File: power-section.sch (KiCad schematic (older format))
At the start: 1 part, among them J1 Screw_Terminal_01x02

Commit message: Added MAX15062 as 3.3V power supply
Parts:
- added C?: C, symbol Device:C
- added C? (x2): 1uF, symbol Device:C
- added L?: 33uH, symbol Device:L
- added U?: MAX15062A, Package_DFN_QFN:DFN-8_2x2mm_P0.5mm, symbol Regulator_Switching:MAX15062A
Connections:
- net labels added: +24V, +3V3, 3.3V
- net labels removed: VCC
- wire segments 6 -> 31
- no-connect marks 0 -> 2
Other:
- moved on the sheet: J1

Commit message: Reorganized everything to use hierarchical sheets in KiCAD. Moved power supply section for motor driver into separate sheet. Moved connectors into top-level sheet
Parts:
- removed J1: Screw_Terminal_01x02, symbol Connector:Screw_Terminal_01x02
- added D1: SSC53L, symbol Device:D_Schottky
- C3: renamed from C?; value C -> 10uF
- gave numbers to parts that had none: 4
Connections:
- net labels added: 3V3, VIN
- net labels removed: +24V, +3V3, 3.3V
- wire segments 31 -> 27
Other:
- moved on the sheet: C1, C2, C3, L1, U1

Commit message: Generated annotations, netlists and assigned footprints into components
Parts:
- C1, C2, C3: footprint (none) -> Capacitor_SMD:C_0805_2012Metric_Pad1.15x1.40mm_HandSolder
- D1: footprint (none) -> Diode_SMD:D_SMC_Handsoldering
- L1: footprint (none) -> Inductor_SMD:L_Coilcraft_LPS4018
- U1: footprint Package_DFN_QFN:DFN-8_2x2mm_P0.5mm -> Package_DFN_QFN:DFN-8-1EP_2x2mm_P0.5mm_EP0.9x1.5mm
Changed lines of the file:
@@
 F 0 "U1" H 6050 4067 50  0000 C CNN
 F 1 "MAX15062A" H 6050 3976 50  0000 C CNN
-F 2 "Package_DFN_QFN:DFN-8_2x2mm_P0.5mm" H 6050 4150 50  0001 C CIN
+F 2 "Package_DFN_QFN:DFN-8-1EP_2x2mm_P0.5mm_EP0.9x1.5mm" H 6050 4150 50  0001 C CIN
 F 3 "http://datasheets.maximintegrated.com/en/ds/MAX15062.pdf" H 6050 3550 50  0001 C CNN
 	1    6050 3600
@@
 F 0 "L1" V 6990 3400 50  0000 C CNN
 F 1 "33uH" V 6899 3400 50  0000 C CNN
-F 2 "" H 6800 3400 50  0001 C CNN
+F 2 "Inductor_SMD:L_Coilcraft_LPS4018" H 6800 3400 50  0001 C CNN
 F 3 "~" H 6800 3400 50  0001 C CNN
 	1    6800 3400
@@
 F 0 "C3" H 7165 4096 50  0000 L CNN
 F 1 "10uF" H 7165 4005 50  0000 L CNN
-F 2 "" H 7088 3900 50  0001 C CNN
+F 2 "Capacitor_SMD:C_0805_2012Metric_Pad1.15x1.40mm_HandSolder" H 7088 3900 50  0001 C CNN
 F 3 "~" H 7050 4050 50  0001 C CNN
 	1    7050 4050
@@
 F 0 "C2" H 5565 4096 50  0000 L CNN
 F 1 "1uF" H 5565 4005 50  0000 L CNN
-F 2 "" H 5488 3900 50  0001 C CNN
+F 2 "Capacitor_SMD:C_0805_2012Metric_Pad1.15x1.40mm_HandSolder" H 5488 3900 50  0001 C CNN
 F 3 "~" H 5450 4050 50  0001 C CNN
 	1    5450 4050
@@
 F 0 "C1" H 5315 3696 50  0000 L CNN
 F 1 "1uF" H 5315 3605 50  0000 L CNN
-F 2 "" H 5238 3500 50  0001 C CNN
+F 2 "Capacitor_SMD:C_0805_2012Metric_Pad1.15x1.40mm_HandSolder" H 5238 3500 50  0001 C CNN
 F 3 "~" H 5200 3650 50  0001 C CNN
 	1    5200 3650
@@
 F 0 "D1" H 4900 3200 50  0000 L CNN
 F 1 "SSC53L" H 4800 3300 50  0000 L CNN
-F 2 "" H 4950 3400 50  0001 C CNN
+F 2 "Diode_SMD:D_SMC_Handsoldering" H 4950 3400 50  0001 C CNN
 F 3 "~" H 4950 3400 50  0001 C CNN
 	1    4950 3400

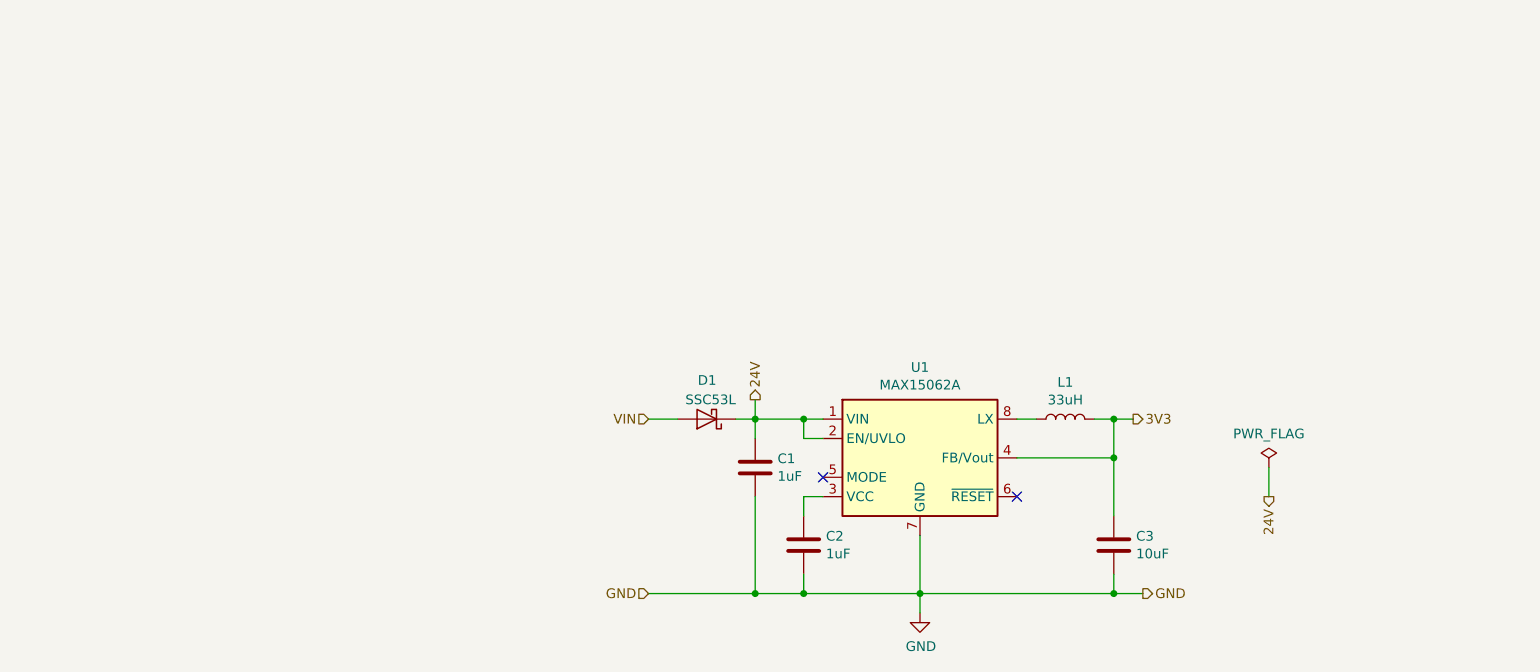
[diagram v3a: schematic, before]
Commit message: Added power supply section to PCB. Added missing components footprints.
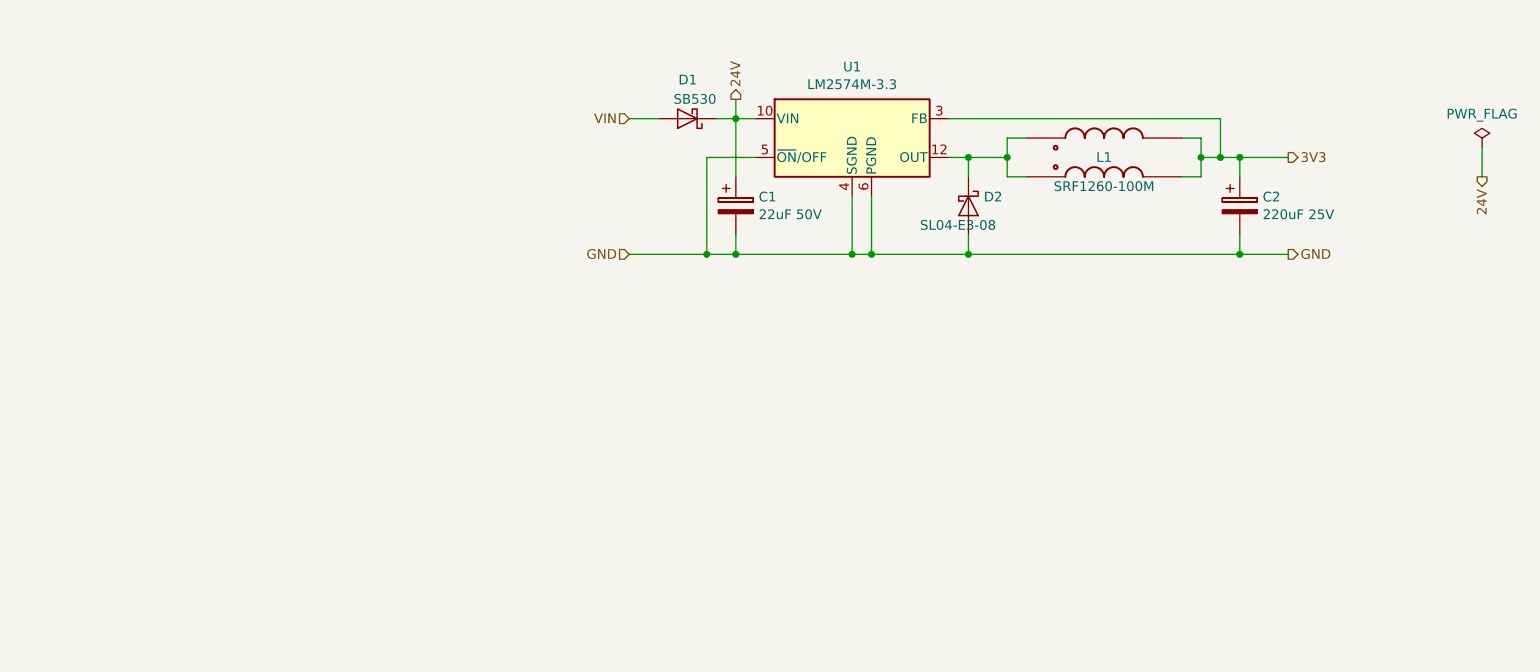
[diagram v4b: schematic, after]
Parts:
- removed C1, C2: 1uF, Capacitor_SMD:C_0805_2012Metric_Pad1.15x1.40mm_HandSolder, symbol Device:C
- removed C3: 10uF, Capacitor_SMD:C_0805_2012Metric_Pad1.15x1.40mm_HandSolder, symbol Device:C
- removed L1: 33uH, Inductor_SMD:L_Coilcraft_LPS4018, symbol Device:L
- removed U1: MAX15062A, Package_DFN_QFN:DFN-8-1EP_2x2mm_P0.5mm_EP0.9x1.5mm, symbol Regulator_Switching:MAX15062A
- added C1: 22uF 50V, Capacitor_THT:CP_Radial_D5.0mm_P2.00mm, symbol Device:CP
- added C2: 220uF 25V, Capacitor_THT:CP_Radial_D6.3mm_P2.50mm, symbol Device:CP
- added D2: SL04-E3-08, Diode_SMD:D_1210_3225Metric_Pad1.42x2.65mm_HandSolder, symbol Device:D_Schottky
- added L1: SRF1260-100M, IND_SRF1260-100M, symbol SRF1260-100M:SRF1260-100M
- added U1: LM2574M-3.3, Package_SO:SOIC-14W_7.5x9.0mm_P1.27mm, symbol Regulator_Switching:LM2574M-3.3
- D1: value SSC53L -> SB530; footprint Diode_SMD:D_SMC_Handsoldering -> Diode_THT:D_DO-201_P3.81mm_Vertical_AnodeUp
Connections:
- net 24V: now also C1.1, U1.10 (VIN)
- net 3V3: now also C2.1, L1.3, L1.4, U1.3 (FB)
- net GND: now also C1.2, C2.2, D2.2 (A), U1.4 (SGND), U1.5 (~ON~/OFF), U1.6 (PGND)
- new net: D2.1 (K), L1.1, L1.2, U1.12 (OUT)
- no-connect marks 2 -> 0
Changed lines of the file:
@@
 Comment4 ""
 $EndDescr
+Text HLabel 7950 2050 2    50   Output ~ 0
+3V3
+Wire Wire Line
+	4550 1850 4700 1850
+Text HLabel 7950 2550 2    50   Output ~ 0
+GND
+Text HLabel 4550 2550 0    50   Input ~ 0
+GND
+Text HLabel 4550 1850 0    50   Input ~ 0
+VIN
+Text HLabel 5100 1750 1    50   Output ~ 0
+24V
 $Comp
-L Regulator_Switching:MAX15062A U1
-U 1 1 5BD97FD1
-P 6050 3600
-F 0 "U1" H 6050 4067 50  0000 C CNN
-F 1 "MAX15062A" H 6050 3976 50  0000 C CNN
-F 2 "Package_DFN_QFN:DFN-8-1EP_2x2mm_P0.5mm_EP0.9x1.5mm" H 6050 4150 50  0001 C CIN
-F 3 "http://datasheets.maximintegrated.com/en/ds/MAX15062.pdf" H 6050 3550 50  0001 C CNN
-	1    6050 3600
+L Device:D_Schottky D1
+U 1 1 5BE562E4
+P 4850 1850
+AR Path="/5BDAF501/5BE562E4" Ref="D1"  Part="1"
+AR Path="/5BE562E4" Ref="D?"  Part="1"
+F 0 "D1" H 4800 1650 50  0000 L CNN
+F 1 "SB530" H 4700 1750 50  0000 L CNN
+F 2 "Diode_THT:D_DO-201_P3.81mm_Vertical_AnodeUp" H 4850 1850 50  0001 C CNN
+F 3 "~" H 4850 1850 50  0001 C CNN
+	1    4850 1850
+	-1   0    0    1
+$EndComp
+$Comp
+L power:PWR_FLAG #FLG01
+U 1 1 5BE562EB
+P 8950 2000
+F 0 "#FLG01" H 8950 2075 50  0001 C CNN
+F 1 "PWR_FLAG" H 8950 2174 50  0000 C CNN
+F 2 "" H 8950 2000 50  0001 C CNN
+F 3 "~" H 8950 2000 50  0001 C CNN
+	1    8950 2000
 	1    0    0    -1
 $EndComp
+Text HLabel 8950 2150 3    50   Output ~ 0
+24V
+Wire Wire Line
+	8950 2150 8950 2000
 $Comp
-L Device:L L1
-U 1 1 5BD98297
-P 6800 3400
-F 0 "L1" V 6990 3400 50  0000 C CNN
-F 1 "33uH" V 6899 3400 50  0000 C CNN
-F 2 "Inductor_SMD:L_Coilcraft_LPS4018" H 6800 3400 50  0001 C CNN
-F 3 "~" H 6800 3400 50  0001 C CNN
-	1    6800 3400
-	0    -1   -1   0
-$EndComp
-Wire Wire Line
-	6550 3400 6650 3400
-$Comp
-L Device:C C3
-U 1 1 5BD98368
-P 7050 4050
-F 0 "C3" H 7165 4096 50  0000 L CNN
-F 1 "10uF" H 7165 4005 50  0000 L CNN
-F 2 "Capacitor_SMD:C_0805_2012Metric_Pad1.15x1.40mm_HandSolder" H 7088 3900 50  0001 C CNN
-F 3 "~" H 7050 4050 50  0001 C CNN
-	1    7050 4050
+L Regulator_Switching:LM2574M-3.3 U1
+U 1 1 5BE562F3
+P 5700 1950
+F 0 "U1" H 5700 2317 50  0000 C CNN
+F 1 "LM2574M-3.3" H 5700 2226 50  0000 C CNN
+F 2 "Package_SO:SOIC-14W_7.5x9.0mm_P1.27mm" H 5300 2300 50  0001 L CIN
+F 3 "http://www.national.com/ds/LM/LM2574.pdf" H 5700 1950 50  0001 C CNN
+	1    5700 1950
 	1    0    0    -1
 $EndComp
 Wire Wire Line
-	6050 4000 6050 4300
-Wire Wire Line
-	6050 4300 7050 4300
-Wire Wire Line
-	7050 4300 7050 4200
+	5000 1850 5100 1850
 $Comp
-L Device:C C2
-U 1 1 5BD984C8
-P 5450 4050
-F 0 "C2" H 5565 4096 50  0000 L CNN
-F 1 "1uF" H 5565 4005 50  0000 L CNN
-F 2 "Capacitor_SMD:C_0805_2012Metric_Pad1.15x1.40mm_HandSolder" H 5488 3900 50  0001 C CNN
-F 3 "~" H 5450 4050 50  0001 C CNN
-	1    5450 4050
+L Device:CP C1
+U 1 1 5BE562FB
+P 5100 2300
+F 0 "C1" H 5218 2346 50  0000 L CNN
+F 1 "22uF 50V" H 5218 2255 50  0000 L CNN
+F 2 "Capacitor_THT:CP_Radial_D5.0mm_P2.00mm" H 5138 2150 50  0001 C CNN
+F 3 "~" H 5100 2300 50  0001 C CNN
+	1    5100 2300
 	1    0    0    -1
 $EndComp
 Wire Wire Line
-	5450 3900 5450 3800
+	5100 2150 5100 1850
+Connection ~ 5100 1850
 Wire Wire Line
-	5450 3800 5550 3800
+	5100 1850 5200 1850
 Wire Wire Line
-	5450 4200 5450 4300
+	4550 2550 4950 2550
 Wire Wire Line
-	5450 4300 6050 4300
-Connection ~ 6050 4300
+	5800 2550 5800 2250
 Wire Wire Line
-	5450 3400 5450 3500
+	5100 2450 5100 2550
+Connection ~ 5100 2550
 Wire Wire Line
-	5450 3500 5550 3500
+	5100 2550 5700 2550
 Wire Wire Line
-	5550 3400 5450 3400
+	5700 2250 5700 2550
+Connection ~ 5700 2550
+Wire Wire Line
+	5700 2550 5800 2550
+Wire Wire Line
+	5200 2050 4950 2050
+Wire Wire Line
+	4950 2050 4950 2550
+Connection ~ 4950 2550
+Wire Wire Line
+	4950 2550 5100 2550
 $Comp
-L Device:C C1
-U 1 1 5BD98908
-P 5200 3650
-F 0 "C1" H 5315 3696 50  0000 L CNN
-F 1 "1uF" H 5315 3605 50  0000 L CNN
-F 2 "Capacitor_SMD:C_0805_2012Metric_Pad1.15x1.40mm_HandSolder" H 5238 3500 50  0001 C CNN
-F 3 "~" H 5200 3650 50  0001 C CNN
-	1    5200 3650
+L Device:D_Schottky D2
+U 1 1 5BE56311
+P 6300 2300
+F 0 "D2" V 6254 2379 50  0000 L CNN
+F 1 "SL04-E3-08" V 6400 2050 50  0000 L CNN
+F 2 "Diode_SMD:D_1210_3225Metric_Pad1.42x2.65mm_HandSolder" H 6300 2300 50  0001 C CNN
+F 3 "~" H 6300 2300 50  0001 C CNN
+	1    6300 2300
+	0    1    1    0
+$EndComp
+Wire Wire Line
+	6200 2050 6300 2050
+Wire Wire Line
+	6300 2050 6300 2150
+Wire Wire Line
+	5800 2550 6300 2550
+Wire Wire Line
+	6300 2550 6300 2450
+Connection ~ 5800 2550
+$Comp
+L Device:CP C2
+U 1 1 5BE5631D
+P 7700 2300
+F 0 "C2" H 7818 2346 50  0000 L CNN
+F 1 "220uF 25V" H 7818 2255 50  0000 L CNN
+F 2 "Capacitor_THT:CP_Radial_D6.3mm_P2.50mm" H 7738 2150 50  0001 C CNN
+F 3 "~" H 7700 2300 50  0001 C CNN
+	1    7700 2300
 	1    0    0    -1
 $EndComp
 Wire Wire Line
-	5200 3500 5200 3400
-Connection ~ 5450 3400
-NoConn ~ 5550 3700
+	7700 2550 7700 2450
+Connection ~ 6300 2050
 Wire Wire Line
-	5200 3800 5200 4300
+	7700 2150 7700 2050
+Connection ~ 7700 2050
 Wire Wire Line
-	5200 4300 5450 4300
-Connection ~ 5450 4300
-NoConn ~ 6550 3800
+	7950 2050 7700 2050
 Wire Wire Line
-	6950 3400 7050 3400
+	5100 1850 5100 1750
 Wire Wire Line
-	7050 3400 7050 3600
-Text HLabel 7150 3400 2    50   Output ~ 0
-3V3
+	7600 2050 7700 2050
+Connection ~ 7700 2550
 Wire Wire Line
-	4650 3400 4800 3400
-Connection ~ 5200 3400
+	7950 2550 7700 2550
 Wire Wire Line
-	7050 3600 6550 3600
-Connection ~ 7050 3600
+	6500 2050 6500 1950
 Wire Wire Line
-	7050 3600 7050 3900
-Text HLabel 7200 4300 2    50   Output ~ 0
-GND
+	6500 1950 6600 1950
 Wire Wire Line
-	7200 4300 7050 4300
-Connection ~ 7050 4300
+	6300 2050 6500 2050
+Wire Wire Line
+	6500 2050 6500 2150
+Wire Wire Line
+	6500 2150 6600 2150
+Connection ~ 6500 2050
+Wire Wire Line
+	7400 1950 7500 1950
+Wire Wire Line
+	7500 1950 7500 2050
+Wire Wire Line
+	7500 2150 7400 2150
+Wire Wire Line
+	7600 1850 7600 2050
+Wire Wire Line
+	7600 2050 7500 2050
+Connection ~ 7500 2050
+Wire Wire Line
+	7500 2050 7500 2150
+Connection ~ 7600 2050
 $Comp
-L power:GND #PWR02
-U 1 1 5BF54359
-P 6050 4400
-F 0 "#PWR02" H 6050 4150 50  0001 C CNN
-F 1 "GND" H 6055 4227 50  0000 C CNN
-F 2 "" H 6050 4400 50  0001 C CNN
-F 3 "" H 6050 4400 50  0001 C CNN
-	1    6050 4400
+L SRF1260-100M:SRF1260-100M L1
+U 1 1 5BE5EC2D
+P 7000 2050
+F 0 "L1" H 7000 2050 50  0000 C CNN
+F 1 "SRF1260-100M" H 7000 1900 50  0000 C CNN
+F 2 "IND_SRF1260-100M" H 7000 2050 50  0001 L BNN
+F 3 "Inductor Power Shielded Wirewound 10uH/40uH 20% 100KHz Ferrite 5.35A/2.67A 24.6mOhm/93.4mOhm DCR T/R" H 7000 2050 50  0001 L BNN
+F 4 "Bourns" H 7000 2050 50  0001 L BNN "Field4"
+F 5 "Nonstandard Bourns" H 7000 2050 50  0001 L BNN "Field5"
+F 6 "SRF1260-100M" H 7000 2050 50  0001 L BNN "Field6"
+F 7 "None" H 7000 2050 50  0001 L BNN "Field7"
+F 8 "Unavailable" H 7000 2050 50  0001 L BNN "Field8"
+	1    7000 2050
 	1    0    0    -1
 $EndComp
 Wire Wire Line
-	6050 4300 6050 4400
+	6300 2550 7700 2550
+Connection ~ 6300 2550
 Wire Wire Line
-	5200 3400 5450 3400
-Connection ~ 7050 3400
-Text HLabel 4650 4300 0    50   Input ~ 0
-GND
-Wire Wire Line
-	5200 4300 4650 4300
-Connection ~ 5200 4300
-Text HLabel 4650 3400 0    50   Input ~ 0
-VIN
-Wire Wire Line
-	7150 3400 7050 3400
-Text HLabel 5200 3300 1    50   Output ~ 0
-24V
-$Comp
-L Device:D_Schottky D1
-U 1 1 5C05D721
-P 4950 3400
-AR Path="/5BDAF501/5C05D721" Ref="D1"  Part="1"
-AR Path="/5C05D721" Ref="D?"  Part="1"
-F 0 "D1" H 4900 3200 50  0000 L CNN
-F 1 "SSC53L" H 4800 3300 50  0000 L CNN
-F 2 "Diode_SMD:D_SMC_Handsoldering" H 4950 3400 50  0001 C CNN
-F 3 "~" H 4950 3400 50  0001 C CNN
-	1    4950 3400
-	-1   0    0    1
-$EndComp
-Wire Wire Line
-	5100 3400 5200 3400
-Wire Wire Line
-	5200 3300 5200 3400
-$Comp
-L power:PWR_FLAG #FLG0101
-U 1 1 5C069F85
-P 7850 3650
-F 0 "#FLG0101" H 7850 3725 50  0001 C CNN
-F 1 "PWR_FLAG" H 7850 3824 50  0000 C CNN
-F 2 "" H 7850 3650 50  0001 C CNN
-F 3 "~" H 7850 3650 50  0001 C CNN
-	1    7850 3650
-	1    0    0    -1
-$EndComp
-Text HLabel 7850 3800 3    50   Output ~ 0
-24V
-Wire Wire Line
-	7850 3800 7850 3650
+	6200 1850 7600 1850
 $EndSCHEMATC

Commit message: PCB creation, improvements of power supply section
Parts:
- L1: footprint IND_SRF1260-100M -> SRF1260-100M:IND_SRF1260-100M
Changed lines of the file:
@@
 F 0 "L1" H 7000 2050 50  0000 C CNN
 F 1 "SRF1260-100M" H 7000 1900 50  0000 C CNN
-F 2 "IND_SRF1260-100M" H 7000 2050 50  0001 L BNN
+F 2 "SRF1260-100M:IND_SRF1260-100M" H 7000 2050 50  0001 L BNN
 F 3 "Inductor Power Shielded Wirewound 10uH/40uH 20% 100KHz Ferrite 5.35A/2.67A 24.6mOhm/93.4mOhm DCR T/R" H 7000 2050 50  0001 L BNN
 F 4 "Bourns" H 7000 2050 50  0001 L BNN "Field4"

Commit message: Further work at PCB
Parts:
- C1: footprint Capacitor_THT:CP_Radial_D5.0mm_P2.00mm -> Capacitor_SMD:CP_Elec_5x5.8
- D1: footprint Diode_THT:D_DO-201_P3.81mm_Vertical_AnodeUp -> PTVS3V3P1UP:SOD128
- D2: footprint Diode_SMD:D_1210_3225Metric_Pad1.42x2.65mm_HandSolder -> Diode_SMD:D_SOD-123F
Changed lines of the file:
@@
 F 0 "D1" H 4800 1650 50  0000 L CNN
 F 1 "SB530" H 4700 1750 50  0000 L CNN
-F 2 "Diode_THT:D_DO-201_P3.81mm_Vertical_AnodeUp" H 4850 1850 50  0001 C CNN
+F 2 "PTVS3V3P1UP:SOD128" H 4850 1850 50  0001 C CNN
 F 3 "~" H 4850 1850 50  0001 C CNN
 	1    4850 1850
@@
 F 0 "C1" H 5218 2346 50  0000 L CNN
 F 1 "22uF 50V" H 5218 2255 50  0000 L CNN
-F 2 "Capacitor_THT:CP_Radial_D5.0mm_P2.00mm" H 5138 2150 50  0001 C CNN
+F 2 "Capacitor_SMD:CP_Elec_5x5.8" H 5138 2150 50  0001 C CNN
 F 3 "~" H 5100 2300 50  0001 C CNN
 	1    5100 2300
@@
 F 0 "D2" V 6254 2379 50  0000 L CNN
 F 1 "SL04-E3-08" V 6400 2050 50  0000 L CNN
-F 2 "Diode_SMD:D_1210_3225Metric_Pad1.42x2.65mm_HandSolder" H 6300 2300 50  0001 C CNN
+F 2 "Diode_SMD:D_SOD-123F" H 6300 2300 50  0001 C CNN
 F 3 "~" H 6300 2300 50  0001 C CNN
 	1    6300 2300
